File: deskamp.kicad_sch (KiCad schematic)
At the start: 0 parts

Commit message: Import ESP32 Mini lib
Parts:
- added U1: mini_esp32, symbol ESP32_mini:mini_esp32
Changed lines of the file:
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@@
 	(generator_version "9.0")
 	(paper "A4")
+	(symbol
+		(lib_id "ESP32_mini:mini_esp32")
+		(at 50.8 38.1 0)
+		(unit 1)
+		(exclude_from_sim no)
+		(in_bom yes)
+		(on_board yes)
+		(dnp no)
+		(fields_autoplaced yes)
+		(property "Reference" "U1"
+			(at 51.435 34.29 0)
+			(effects
+				(font
+					(size 1.27 1.27)
+				)
+			)
+		)
+		(property "Value" "mini_esp32"
+			(at 51.435 36.83 0)
+			(effects
+				(font
+					(size 1.27 1.27)
+				)
+			)
+		)
+		(property "Footprint" ""
+			(at 54.61 35.56 0)
+			(effects
+				(font
+					(size 1.27 1.27)
+				)
+				(hide yes)
+			)
+		)
+		(property "Datasheet" ""
+			(at 54.61 35.56 0)
+			(effects
+				(font
+					(size 1.27 1.27)
+				)
+				(hide yes)
+			)
+		)
+		(property "Description" ""
+			(at 50.8 38.1 0)
+			(effects
+				(font
+					(size 1.27 1.27)
+				)
+				(hide yes)
+			)
+		)
+		(pin "4"
+		)
+		(pin "5"
+		)
+		(pin "1"
+		)
+		(pin "2"
+		)
+		(pin "3"
+		)
+		(pin "34"
+		)
+		(pin "36"
+		)
+		(pin "32"
+		)
+		(pin "18"
+		)
+		(pin "13"
+		)
+		(pin "31"
+		)
+		(pin "29"
+		)
+		(pin "8"
+		)
+		(pin "20"
+		)
+		(pin "30"
+		)
+		(pin "10"
+		)
+		(pin "28"
+		)
+		(pin "9"
+		)
+		(pin "11"
+		)
+		(pin "7"
+		)
+		(pin "27"
+		)
+		(pin "25"
+		)
+		(pin "12"
+		)
+		(pin "26"
+		)
+		(pin "6"
+		)
+		(pin "24"
+		)
+		(pin "35"
+		)
+		(pin "16"
+		)
+		(pin "33"
+		)
+		(pin "22"
+		)
+		(pin "15"
+		)
+		(pin "19"
+		)
+		(pin "21"
+		)
+		(pin "23"
+		)
+		(pin "40"
+		)
+		(pin "39"
+		)
+		(pin "38"
+		)
+		(pin "37"
+		)
+		(pin "14"
+		)
+		(pin "17"
+		)
+		(instances
+			(project ""
+				(path "/59ddc706-9eaa-4fe8-a820-1bc51705c457"
+					(reference "U1")
+					(unit 1)
+				)
+			)
+		)
+	)
 	(sheet_instances
 		(path "/"

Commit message: Start building switch logic
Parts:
- removed U1: mini_esp32, symbol ESP32_mini:mini_esp32
- added D1, D2, D3, D4: 1N4004, Diode_THT:D_DO-41_SOD81_P10.16mm_Horizontal, symbol Diode:1N4004
- added J1, J2, J3: Conn_01x04_Pin, Connector_JST:JST_XH_B4B-XH-AM_1x04_P2.50mm_Vertical, symbol Connector:Conn_01x04_Pin
- added K1, K2: Relay_SPST-NC, symbol Relay:Relay_SPST-NC
- added K3, K4: TQ2-12V, RELAY_TQ2_PAN, symbol 2025-10-05_02-56-43:TQ2-12V
- added Q1, Q2: 2N7000, Package_TO_SOT_THT:TO-92L_HandSolder, symbol Transistor_FET:2N7000
- added U1: esp32-wemos-d1-mini, esp32-wemos-d1-mini:esp32-wemos-d1-mini, symbol esp32-wemos-d1-mini:esp32-wemos-d1-mini
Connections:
- new net: D2.2 (A), K2.A1
- new net: D2.1 (K), K2.A2
- new net: J2.1 (Pin_1), K4.8
- new net: J2.2 (Pin_2), K4.3
- new net: J1.1 (Pin_1), K3.8
- new net: J1.2 (Pin_2), K3.3
- new net: D4.2 (A), K4.10
- new net: D1.2 (A), K1.A1
- new net: D1.1 (K), K1.A2
- new net: D3.2 (A), K3.10
- new net: J3.3 (Pin_3), K3.4, K4.4
- new net: J3.4 (Pin_4), K3.7, K4.7
- new net +12V: D3.1 (K), D4.1 (K), K3.1, K4.1
- new net GNDA: J1.3 (Pin_3), J1.4 (Pin_4), J2.3 (Pin_3), J2.4 (Pin_4), J3.1 (Pin_1), J3.2 (Pin_2)
- no-connect marks 0 -> 8

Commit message: Start building frontend
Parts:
- removed D1, D2: 1N4004, Diode_THT:D_DO-41_SOD81_P10.16mm_Horizontal, symbol Diode:1N4004
- removed K1, K2: Relay_SPST-NC, symbol Relay:Relay_SPST-NC
- added C1: 10µF, Capacitor_SMD:CP_Elec_6.3x5.4_Nichicon, symbol Device:C_Polarized
- added J4: Selector Switch, symbol Connector:Conn_01x03_Pin
- added J5: LFE, Connector_JST:JST_XH_B2B-XH-AM_1x02_P2.50mm_Vertical, symbol Connector:Conn_01x02_Pin
- added K1, K2: Relay_SPDT, Relay_THT:Relay_SPDT_Panasonic_JW1_FormC, symbol Relay:Relay_SPDT
- added R1, R2: 100K, Resistor_THT:R_Axial_DIN0204_L3.6mm_D1.6mm_P5.08mm_Horizontal, symbol Device:R
- J1: value Conn_01x04_Pin -> Input 01
- J2: value Conn_01x04_Pin -> Input 02
- J3: value Conn_01x04_Pin -> Preamp Out
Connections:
- net at J1.1 (Pin_1), K3.8: now also Q1.3 (D)
- net at D4.2 (A), K4.10: now also Q2.3 (D), C1.1
- net GND: now reaches Q2.1 (S)
- net GND: now also Q1.1 (S), U1.1 (GND), C1.2, J4.3 (Pin_3)
- net at Q2.2 (G): now also U1.29 (IO_17/D3)
- net at Q1.2 (G): now also U1.31 (IO_16/D4)
- net at U1.10 (IO_19/D6): now also J4.2 (Pin_2), R1.2
- net +3V3: now reaches U1.16 (3V3)
- net +3V3: now also R1.1, R2.1
- net at U1.8 (IO_18/D5): now also J4.1 (Pin_1), R2.2
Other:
- moved on the sheet: Q1, Q2, U1

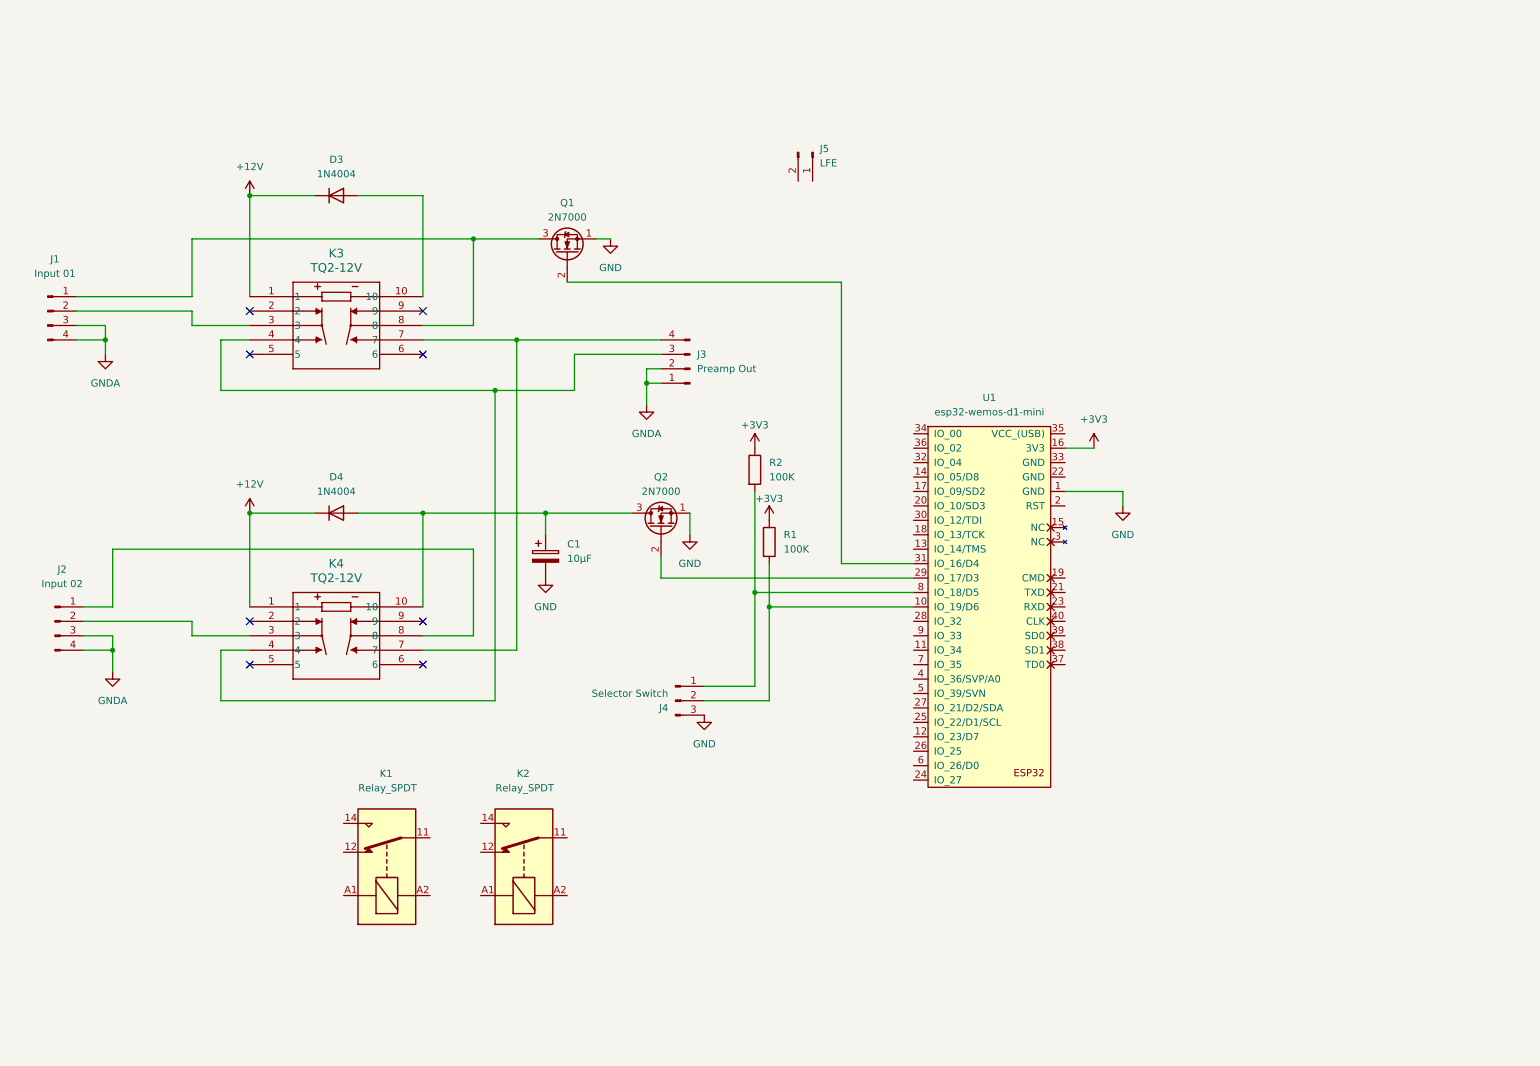
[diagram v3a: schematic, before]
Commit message: Fix flyback diodes, add amp relays
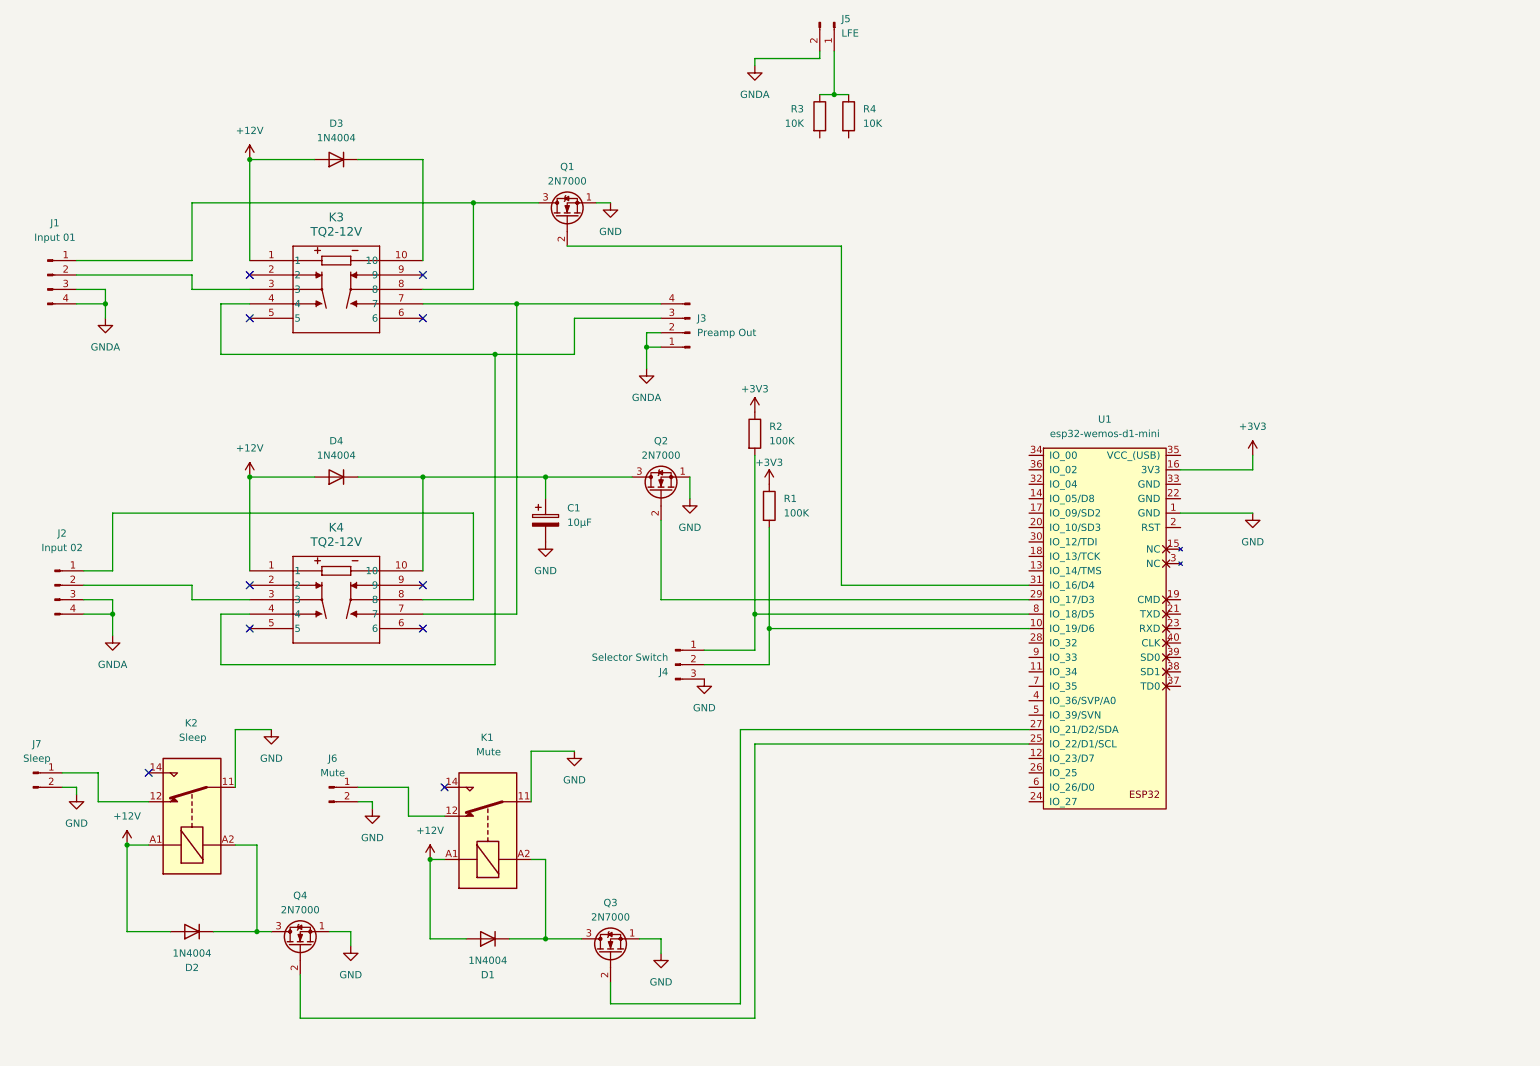
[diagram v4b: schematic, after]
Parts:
- added D1, D2: 1N4004, Diode_THT:D_DO-41_SOD81_P10.16mm_Horizontal, symbol Diode:1N4004
- added J6: Mute, symbol Connector:Conn_01x02_Pin
- added J7: Sleep, symbol Connector:Conn_01x02_Pin
- added Q3, Q4: 2N7000, Package_TO_SOT_THT:TO-92L_HandSolder, symbol Transistor_FET:2N7000
- added R3, R4: 10K, OptoDevice:R_LDR_5.2x5.2mm_P3.5mm_Horizontal, symbol Device:R
- K1: value Relay_SPDT -> Mute
- K2: value Relay_SPDT -> Sleep
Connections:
- net +12V: now also D3.2 (A), D4.2 (A), K1.A1, K2.A1, D1.2 (A), D2.2 (A); no longer D3.1 (K), D4.1 (K)
- net GND: now also K1.11, K2.11, J6.2 (Pin_2), J7.2 (Pin_2), Q3.1 (S), Q4.1 (S)
- net GNDA: now also J5.2 (Pin_2)
- net at J5.1 (Pin_1): now also R3.1, R4.1
- net at K1.12: now also J6.1 (Pin_1)
- net at K1.A2: now also D1.1 (K), Q3.3 (D)
- net at C1.1, K4.10, Q2.3 (D): now also D4.1 (K); no longer D4.2 (A)
- net at K2.12: now also J7.1 (Pin_1)
- net at K2.A2: now also D2.1 (K), Q4.3 (D)
- net at K3.10: now also D3.1 (K); no longer D3.2 (A)
- net at U1.25 (IO_22/D1/SCL): now also Q4.2 (G)
- net at U1.27 (IO_21/D2/SDA): now also Q3.2 (G)
- no-connect marks 8 -> 10
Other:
- moved on the sheet: C1, D3, D4, J1, J2, J3, J4, J5, K1, K2, K3, K4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

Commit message: Add potentiometer
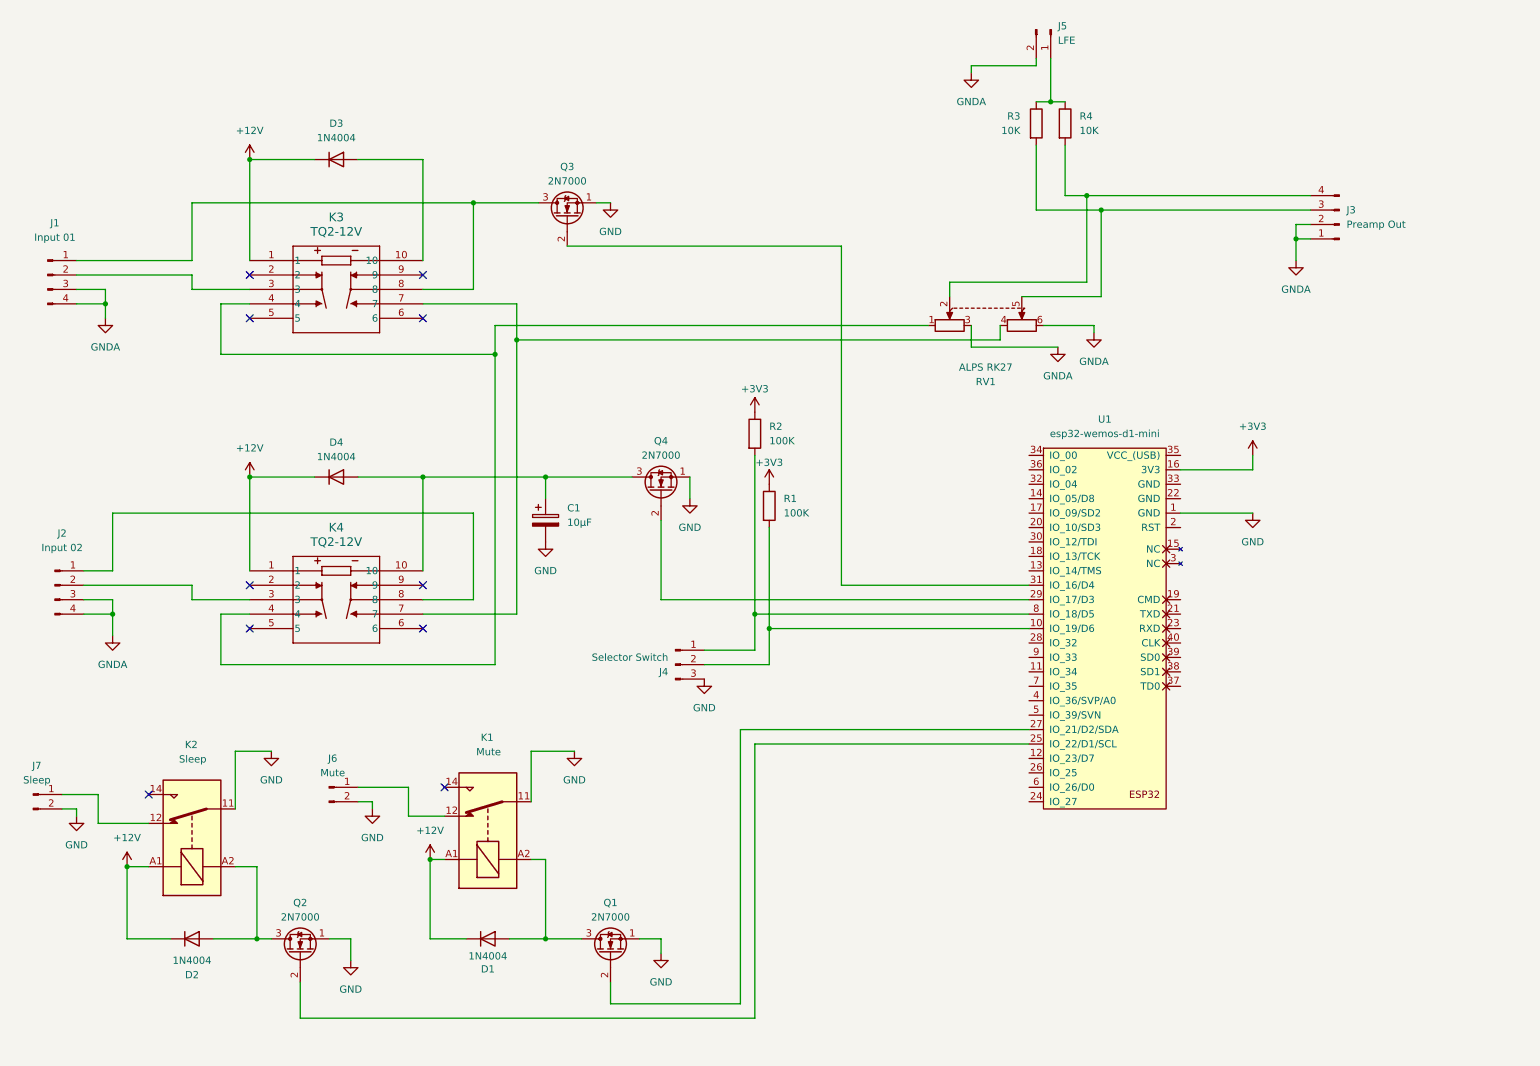
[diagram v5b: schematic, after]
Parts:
- added RV1: ALPS RK27, symbol Device:R_Potentiometer_Dual
- renumbered Q3 to Q1, Q4 to Q2, Q1 to Q3, Q2 to Q4
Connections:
- net +12V: now also D1.1 (K), D2.1 (K), D3.1 (K), D4.1 (K); no longer D1.2 (A), D2.2 (A), D3.2 (A), D4.2 (A)
- net GNDA: now also RV1.3, RV1.6
- net at K1.A2, Q1.3 (D): now also D1.2 (A); no longer D1.1 (K)
- net at C1.1, K4.10, Q4.3 (D): now also D4.2 (A); no longer D4.1 (K)
- net at K2.A2, Q2.3 (D): now also D2.2 (A); no longer D2.1 (K)
- net at K3.10: now also D3.2 (A); no longer D3.1 (K)
- net at K3.4, K4.4: now also RV1.1; no longer J3.3 (Pin_3)
- net at K3.7, K4.7: now also RV1.4; no longer J3.4 (Pin_4)
- net at R3.2: now also J3.3 (Pin_3), RV1.5
- net at R4.2: now also J3.4 (Pin_4), RV1.2
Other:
- moved on the sheet: D1, D2, D3, D4, J3, J5, J7, K2, Q2, R3, R4

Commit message: Add 3.3V regulator
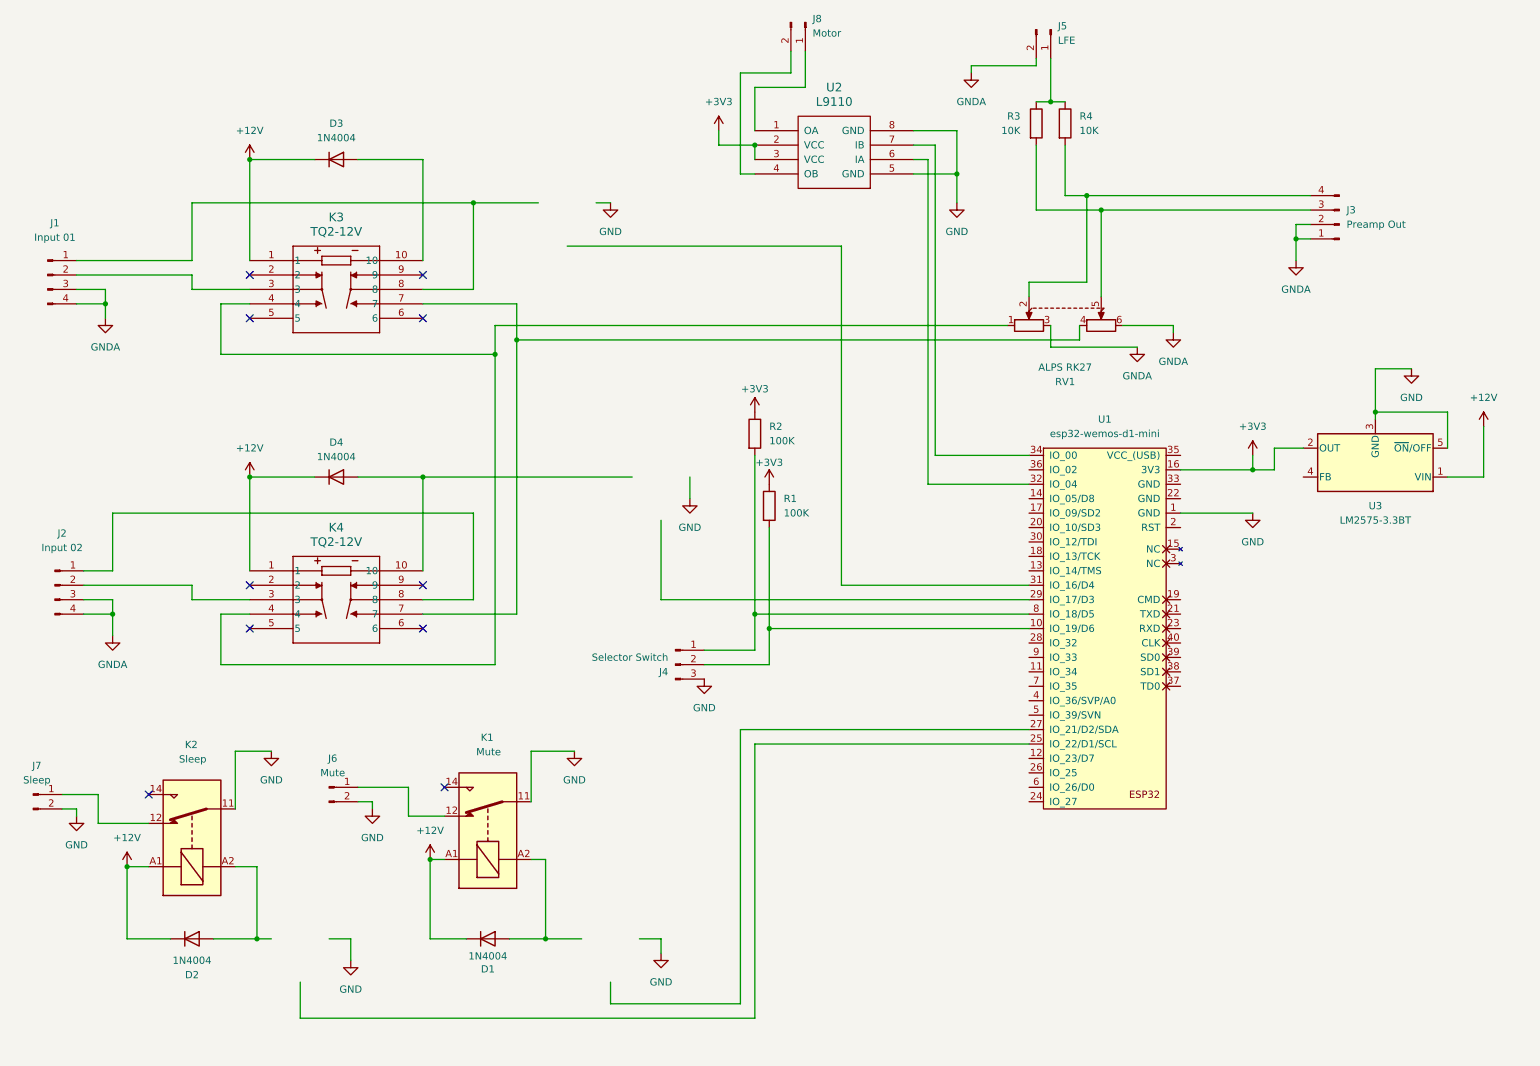
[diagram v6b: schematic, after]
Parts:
- removed C1: 10µF, Capacitor_SMD:CP_Elec_6.3x5.4_Nichicon, symbol Device:C_Polarized
- removed Q1, Q2, Q3, Q4: 2N7000, Package_TO_SOT_THT:TO-92L_HandSolder, symbol Transistor_FET:2N7000
- added J8: Motor, symbol Connector:Conn_01x02_Pin
- added U2: L9110, symbol L9110:L9110
- added U3: LM2575-3.3BT, Package_TO_SOT_THT:TO-220-5_Vertical, symbol Regulator_Switching:LM2575-3.3BT
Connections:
- net +12V: now also U3.1 (VIN)
- net +3V3: now also U2.2 (VCC), U2.3 (VCC), U3.2 (OUT)
- net GND: now also U2.5 (GND), U2.8 (GND), U3.3 (GND), U3.5 (~{ON}/OFF)
- net at U1.32 (IO_04): now also U2.6 (IA)
- net at U1.34 (IO_00): now also U2.7 (IB)
- new net: J8.1 (Pin_1), U2.1 (OA)
- new net: J8.2 (Pin_2), U2.4 (OB)
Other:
- moved on the sheet: RV1
